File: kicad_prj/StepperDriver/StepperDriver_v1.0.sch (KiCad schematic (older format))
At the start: 15 parts

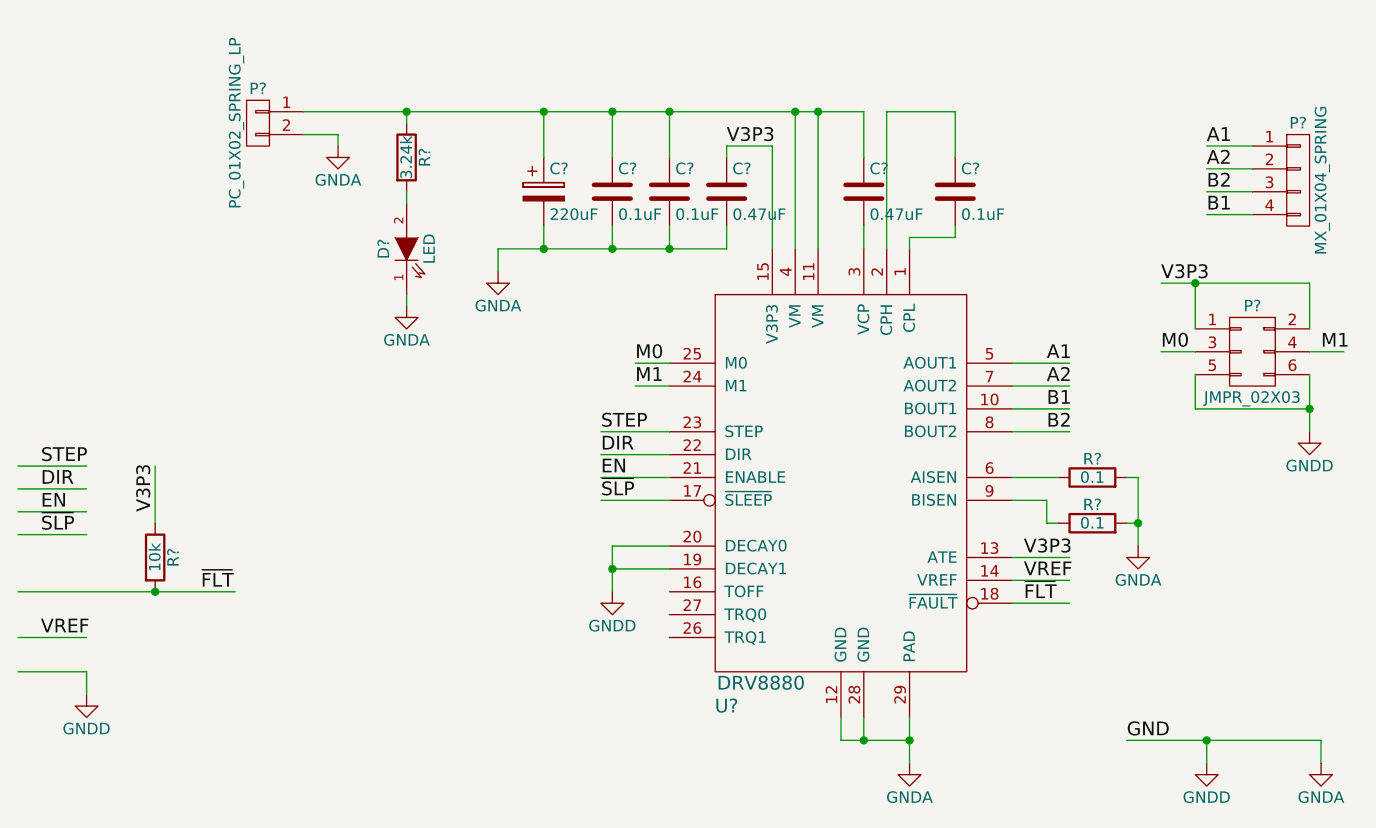
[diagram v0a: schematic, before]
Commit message: Pads minor change
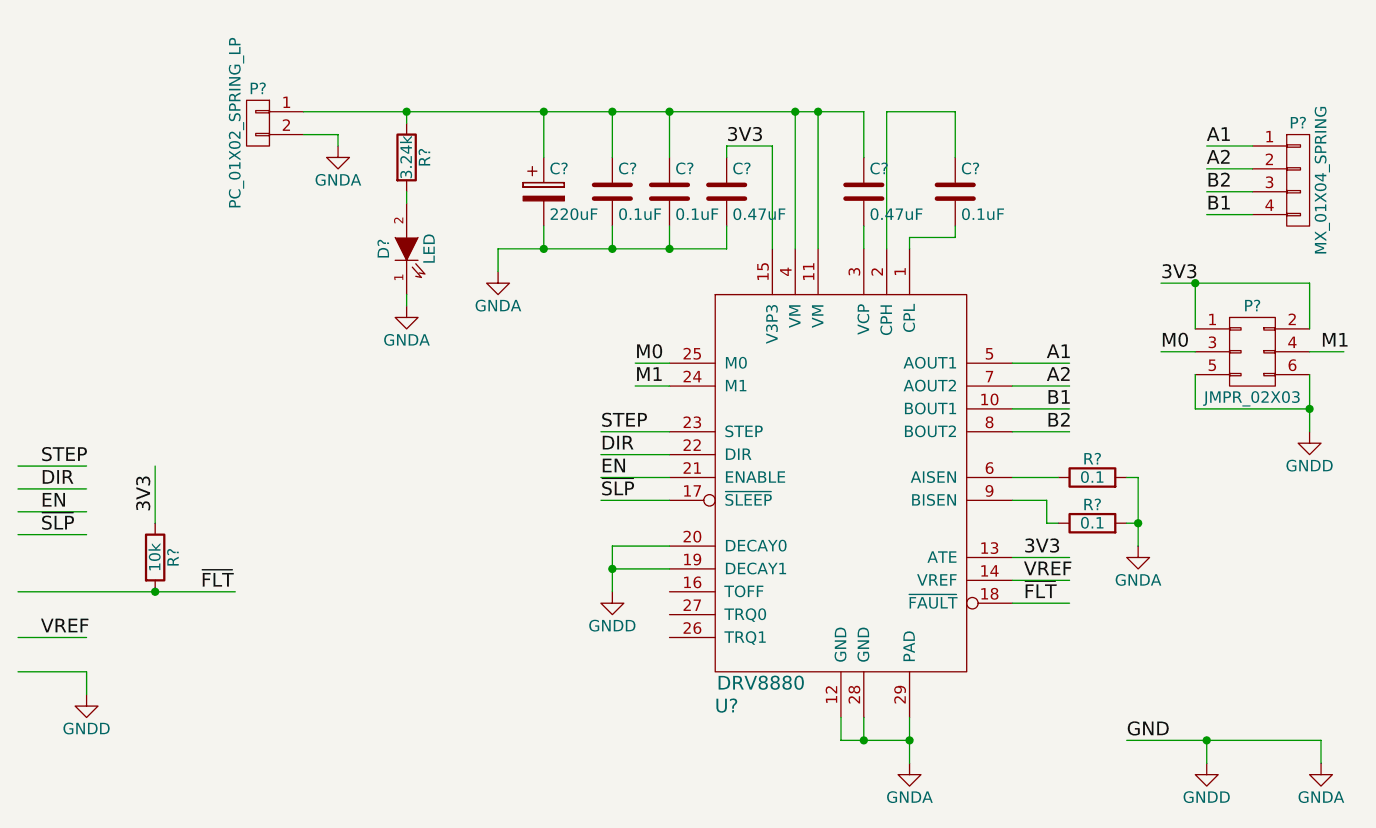
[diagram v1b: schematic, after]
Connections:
- net labels added: 3V3
- net labels removed: V3P3
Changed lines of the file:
@@
 Connection ~ 6100 5150
 Text Label 5300 2550 0    60   ~ 0
-V3P3
+3V3
 Wire Wire Line
 	3450 2400 3900 2400
@@
 	6550 4350 6800 4350
 Text Label 6600 4350 0    60   ~ 0
-V3P3
+3V3
 Wire Wire Line
 	5050 4300 4800 4300
@@
 Connection ~ 7350 3150
 Text Label 7200 3150 0    60   ~ 0
-V3P3
+3V3
 $Comp
 L GNDD #PWR05
@@
 	2800 4200 2800 3950
 Text Label 2800 4150 1    60   ~ 0
-V3P3
+3V3
 Text Label 3000 4500 0    60   ~ 0
 ~FLT

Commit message: Some changes
Don't remember
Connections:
- net labels removed: ~SLP
- wire segments 96 -> 94
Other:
- moved on the sheet: R?
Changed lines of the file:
@@
 L R R?
 U 1 1 56534F8B
-P 2800 4350
+P 2800 4100
 AR Path="/56526EA5/56534F8B" Ref="R?"  Part="1"
 AR Path="/5653D417/56534F8B" Ref="R?"  Part="1"
 AR Path="/5654C1EE/56534F8B" Ref="R?"  Part="1"
 AR Path="/56542384/56534F8B" Ref="R?"  Part="1"
-F 0 "R?" V 2880 4350 50  0000 C CNN
-F 1 "10k" V 2800 4350 50  0000 C CNN
-F 2 "" V 2730 4350 30  0000 C CNN
-F 3 "" H 2800 4350 30  0000 C CNN
-	1    2800 4350
+F 0 "R?" V 2880 4100 50  0000 C CNN
+F 1 "10k" V 2800 4100 50  0000 C CNN
+F 2 "" V 2730 4100 30  0000 C CNN
+F 3 "" H 2800 4100 30  0000 C CNN
+	1    2800 4100
 	1    0    0    -1
 $EndComp
@@
 Wire Wire Line
 	5050 4000 4750 4000
-Wire Wire Line
-	5050 4100 4750 4100
 Text Label 4750 3800 0    60   ~ 0
 STEP
@@
 Text Label 4750 4000 0    60   ~ 0
 EN
-Text Label 4750 4100 0    60   ~ 0
-~SLP
 Wire Wire Line
 	2200 3950 2500 3950
@@
 	2200 4150 2500 4150
 Wire Wire Line
-	2200 4250 2500 4250
+	2200 4250 2800 4250
 Wire Wire Line
-	2200 4500 2800 4500
+	2800 4250 3150 4250
 Wire Wire Line
-	2800 4500 3150 4500
+	3850 4950 4150 4950
+Connection ~ 2800 4250
 Wire Wire Line
-	2200 4700 2500 4700
-Connection ~ 2800 4500
-Wire Wire Line
-	2800 4200 2800 3950
-Text Label 2800 4150 1    60   ~ 0
+	2800 3950 2800 3700
+Text Label 2800 3850 1    60   ~ 0
 3V3
-Text Label 3000 4500 0    60   ~ 0
+Text Label 3000 4250 0    60   ~ 0
 ~FLT
 Text Label 2300 3950 0    60   ~ 0
@@
 Text Label 2300 4150 0    60   ~ 0
 EN
-Text Label 2300 4250 0    60   ~ 0
-~SLP
-Text Label 2300 4700 0    60   ~ 0
+Text Label 3950 4950 0    60   ~ 0
 VREF
 $Comp
@@
 GND
 Wire Wire Line
-	2200 4850 2500 4850
+	2200 4350 2500 4350
 Wire Wire Line
-	2500 4850 2500 4950
+	2500 4350 2500 4450
 $Comp
 L GNDD #PWR?
 U 1 1 5709A053
-P 2500 4950
-F 0 "#PWR?" H 2500 4700 50  0001 C CNN
-F 1 "GNDD" H 2500 4800 50  0000 C CNN
-F 2 "" H 2500 4950 60  0000 C CNN
-F 3 "" H 2500 4950 60  0000 C CNN
-	1    2500 4950
+P 2500 4450
+F 0 "#PWR?" H 2500 4200 50  0001 C CNN
+F 1 "GNDD" H 2500 4300 50  0000 C CNN
+F 2 "" H 2500 4450 60  0000 C CNN
+F 3 "" H 2500 4450 60  0000 C CNN
+	1    2500 4450
 	1    0    0    -1
 $EndComp
